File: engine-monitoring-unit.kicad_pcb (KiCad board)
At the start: 4 copper layers, 70 x 50 mm, 60 parts, among them J1 SW Debug, J2 Supply, J3 Oil Temperature, J4 Air Temperature, J5 Wheel Speed, J6 Inductive Sensor Wire, Q1 MMBT3904, U1 LMR16006XDDCR, U2 STM32F411CEU6, Y1 HSE, Y2 LSE

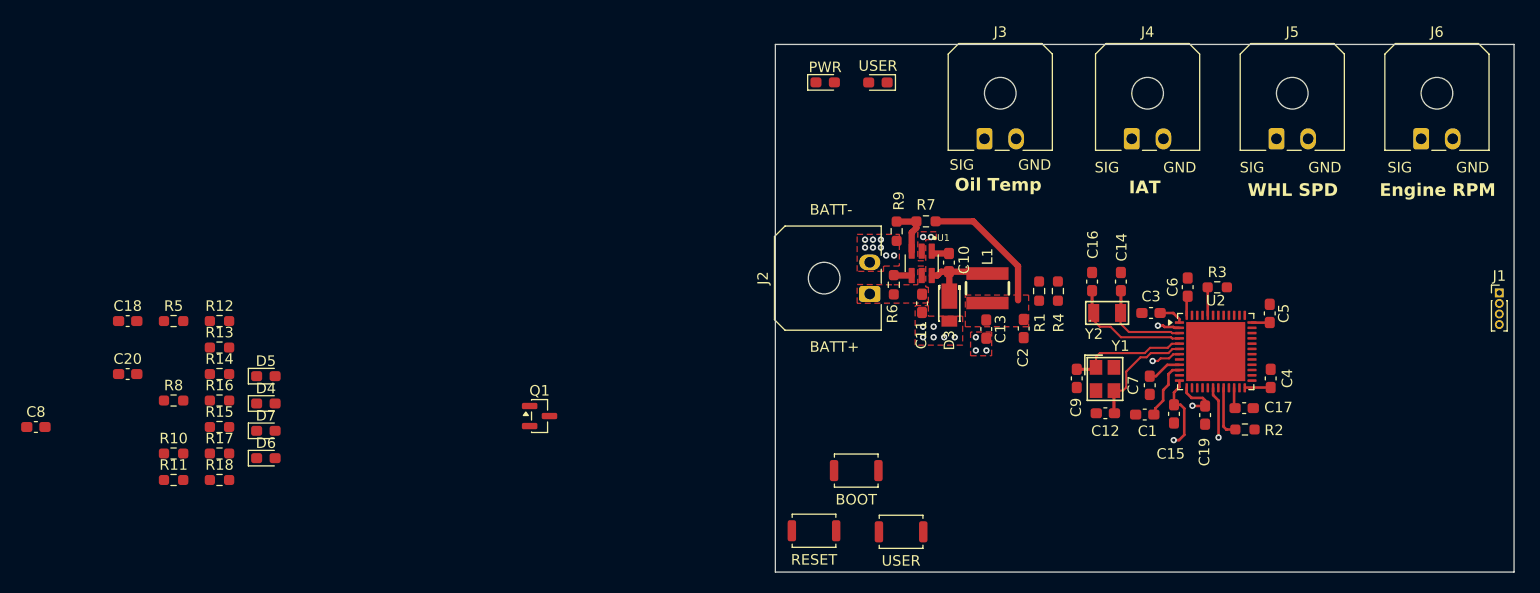
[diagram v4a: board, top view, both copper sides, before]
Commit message: Routed Signal Traces
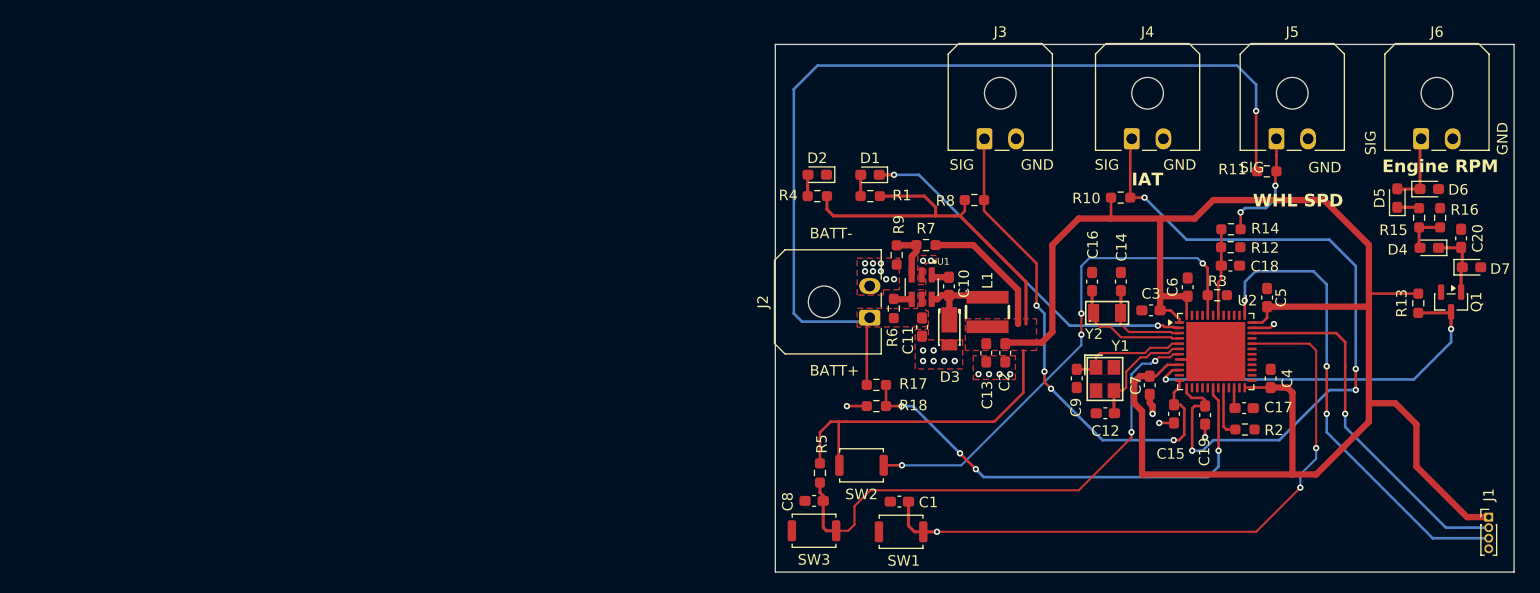
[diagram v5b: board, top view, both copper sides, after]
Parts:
- D1: renamed from USER; value LED_PWR -> LED_USER
- D2: renamed from PWR; value LED_USER -> LED_PWR
- moved C20 127.0 mm to (185.0, 118.4), turned to 90 degrees
- moved R16 117.0 mm to (183.0, 116.4), turned to 90 degrees
- moved R15 115.4 mm to (181.0, 116.4), turned to 90 degrees
- moved D7 115.3 mm to (186.0, 121.1)
- moved R13 113.7 mm to (180.9, 124.5), turned to -90 degrees
- moved D6 113.2 mm to (182.0, 113.7)
- moved D4 111.2 mm to (182.0, 119.3), turned to 180 degrees
- moved D5 108.5 mm to (178.9, 114.6), turned to 90 degrees
- moved R11 107.6 mm to (166.6, 112.0)
- moved C18 104.6 mm to (163.1, 121.0)
- moved R14 96.8 mm to (163.2, 117.5), turned to 180 degrees
- moved R12 96.1 mm to (163.2, 119.2)
- moved R10 93.0 mm to (152.7, 114.5)
- moved Q1 87.1 mm to (184.0, 124.4), turned to -90 degrees
- moved R8 78.2 mm to (138.9, 114.7)
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- renumbered USER to SW1, BOOT to SW2, RESET to SW3
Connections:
- C1 pad 2: /PA0 -> /PA11
- SW1 pad 1: /PA0 -> /PA11
- U2 pad 32: unconnected-(U2-PA11-Pad32) -> /PA11
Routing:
- net +3.3V: track 24.2 -> 245.3 mm
- net VIN: track 0.00 -> 89.1 mm, vias 0 -> 1
- net /PA3: track 4.27 -> 67.7 mm, vias 1 -> 4
- net /PA11: track 0.00 -> 61.4 mm, vias 0 -> 3
- net /NRST: track 2.80 -> 49.9 mm, vias 1 -> 2
- net /BOOT0: track 2.66 -> 48.1 mm, vias 0 -> 4
- net /PA14: track 0.00 -> 45.4 mm, vias 0 -> 3
- net /PA2: track 7.33 -> 47.3 mm, vias 1 -> 4
- net /PB0: track 4.92 -> 44.4 mm, vias 1 -> 4
- net /PA13: track 0.00 -> 34.8 mm, vias 0 -> 1
- net /PC13: track 2.13 -> 34.5 mm, vias 1 -> 2
- net /PA0: track 5.67 -> 36.2 mm, vias 0 -> 2
- net GND: track 0.00 -> 12.4 mm, vias 19 -> 25
- net Net-(J5-Pin_1): track 0.00 -> 11.1 mm, vias 0 -> 2
- net /PB6: track 0.00 -> 7.75 mm
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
